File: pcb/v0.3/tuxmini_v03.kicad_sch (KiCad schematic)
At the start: 80 parts, among them J1 USB_C_Receptacle_USB2.0_16P, J3 Conn_01x09, J4 Conn_01x10, J6 Conn_01x02, J7 Conn_01x02, J8 Conn_01x03, Q1 DMG1045U, Q2 Si2301CDS, Q3 2N7002, SW1 Boot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

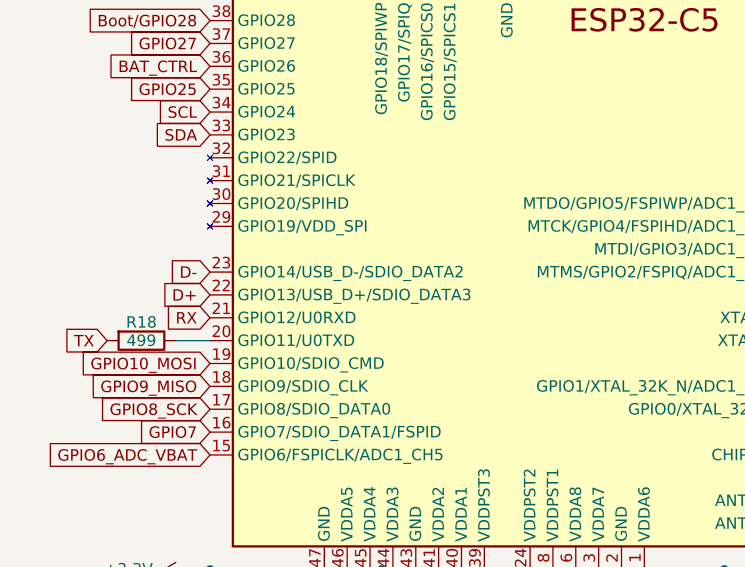
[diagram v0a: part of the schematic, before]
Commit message: Swaped D- and D+ pin on ESP32-C5 pinout
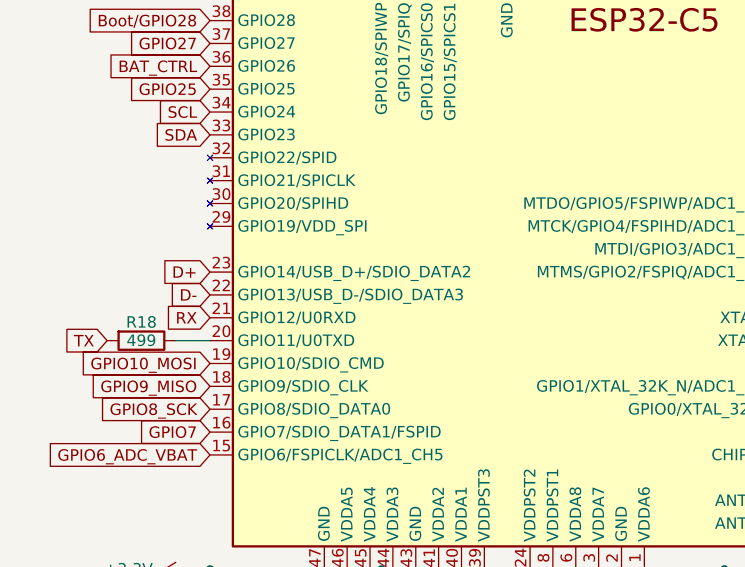
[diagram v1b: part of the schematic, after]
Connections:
- net D+: now also U1.23 (GPIO14/USB_D+/SDIO_DATA2); no longer U1.22 (GPIO13/USB_D+/SDIO_DATA3)
- net D-: now also U1.22 (GPIO13/USB_D-/SDIO_DATA3); no longer U1.23 (GPIO14/USB_D-/SDIO_DATA2)
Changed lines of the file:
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@@
+		)
+	)
+	(global_label "D+"
+		(shape input)
+		(at 33.02 58.42 180)
+		(fields_autoplaced yes)
+		(effects
+			(font
+				(size 1.27 1.27)
+			)
+			(justify right)
+		)
+		(property "Intersheetrefs" "${INTERSHEET_REFS}"
+			(at 27.1924 58.42 0)
+			(effects
+				(font
+					(size 1.27 1.27)
+				)
+				(justify right)
+				(hide yes)
+			)
 		)
 	)
@@
 		)
 	)
+	(global_label "D-"
+		(shape input)
+		(at 33.02 60.96 180)
+		(fields_autoplaced yes)
+		(effects
+			(font
+				(size 1.27 1.27)
+			)
+			(justify right)
+		)
+		(property "Intersheetrefs" "${INTERSHEET_REFS}"
+			(at 27.1924 60.96 0)
+			(effects
+				(font
+					(size 1.27 1.27)
+				)
+				(justify right)
+				(hide yes)
+			)
+		)
+	)
 	(global_label "GPIO8_SCK"
 		(shape input)
@@
 				)
 				(justify left)
-				(hide yes)
-			)
-		)
-	)
-	(global_label "D+"
-		(shape input)
-		(at 33.02 60.96 180)
-		(fields_autoplaced yes)
-		(effects
-			(font
-				(size 1.27 1.27)
-			)
-			(justify right)
-		)
-		(property "Intersheetrefs" "${INTERSHEET_REFS}"
-			(at 27.1924 60.96 0)
-			(effects
-				(font
-					(size 1.27 1.27)
-				)
-				(justify right)
 				(hide yes)
 			)
@@
 				(hide yes)
 			)
-		)
-	)
-	(global_label "D-"
-		(shape input)
-		(at 33.02 58.42 180)
-		(fields_autoplaced yes)
-		(effects
-			(font
-				(size 1.27 1.27)
-			)
-			(justify right)
-		)
-		(property "Intersheetrefs" "${INTERSHEET_REFS}"
-			(at 27.1924 58.42 0)
-			(effects
-				(font
-					(size 1.27 1.27)
-				)
-				(justify right)
-				(hide yes)
-			)
